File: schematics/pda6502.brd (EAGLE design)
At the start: 100 x 80 mm, 40 parts, among them IC1 74HC00D, IC2 74HC138D, IC3 DS1813-SMD, J1 CON_HEADER_2X07-PTH, U1 W65C02S, U2 W65C22S, U3 28C256, U4 UM61256AK-12

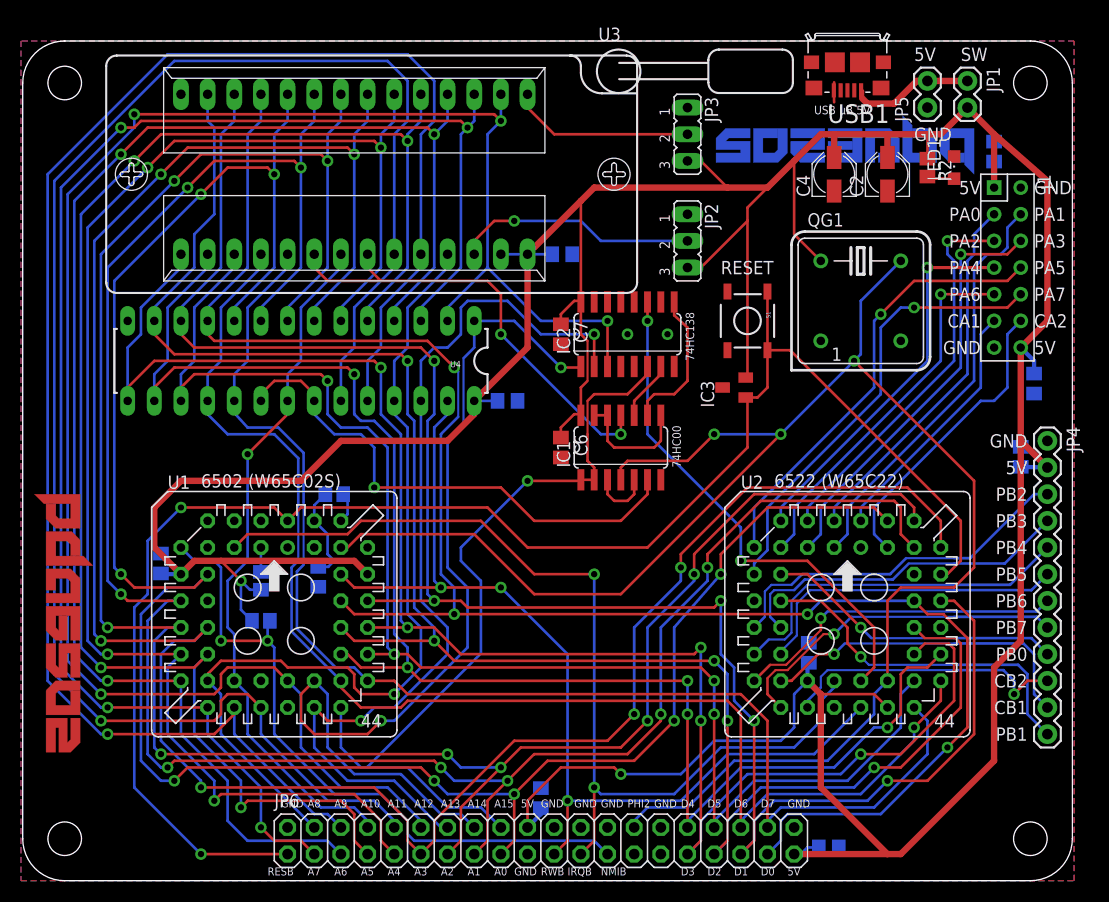
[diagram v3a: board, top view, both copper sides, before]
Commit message: board: silkscreen labelling; ~90% done.
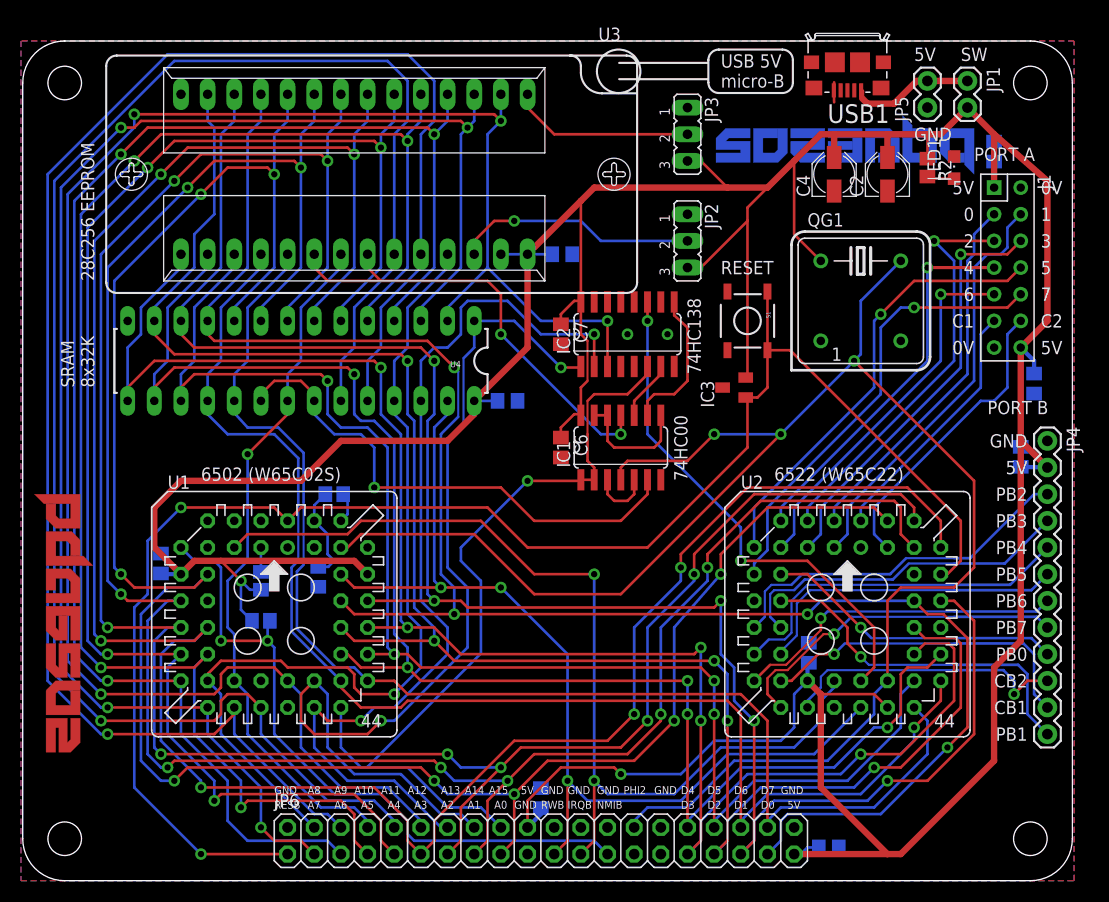
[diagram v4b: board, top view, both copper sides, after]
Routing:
- net PA2: track 37.2 -> 39.0 mm
- net RWB: track 94.5 -> 95.3 mm
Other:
- board text added: "0"
- board text added: "0V"
- board text added: "1"
- board text added: "2"
- board text added: "28C256 EEPROM"
- board text added: "3"
- board text added: "4"
- board text added: "5"
- board text added: "6"
- board text added: "7"
- board text added: "C1"
- board text added: "C2"
- board text added: "PORT A"
- board text added: "PORT B"
- board text added: "SRAM 8x32K"
- board text added: "USB 5V micro-B"
- board text removed: "CA1"
- board text removed: "CA2"
- board text removed: "PA0"
- board text removed: "PA1"
- board text removed: "PA2"
- board text removed: "PA3"
- board text removed: "PA4"
- board text removed: "PA5"
- board text removed: "PA6"
- board text removed: "PA7"
- board text removed: "USB µB 5V"

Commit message: schematics, board: labelling, tweaks, polish.
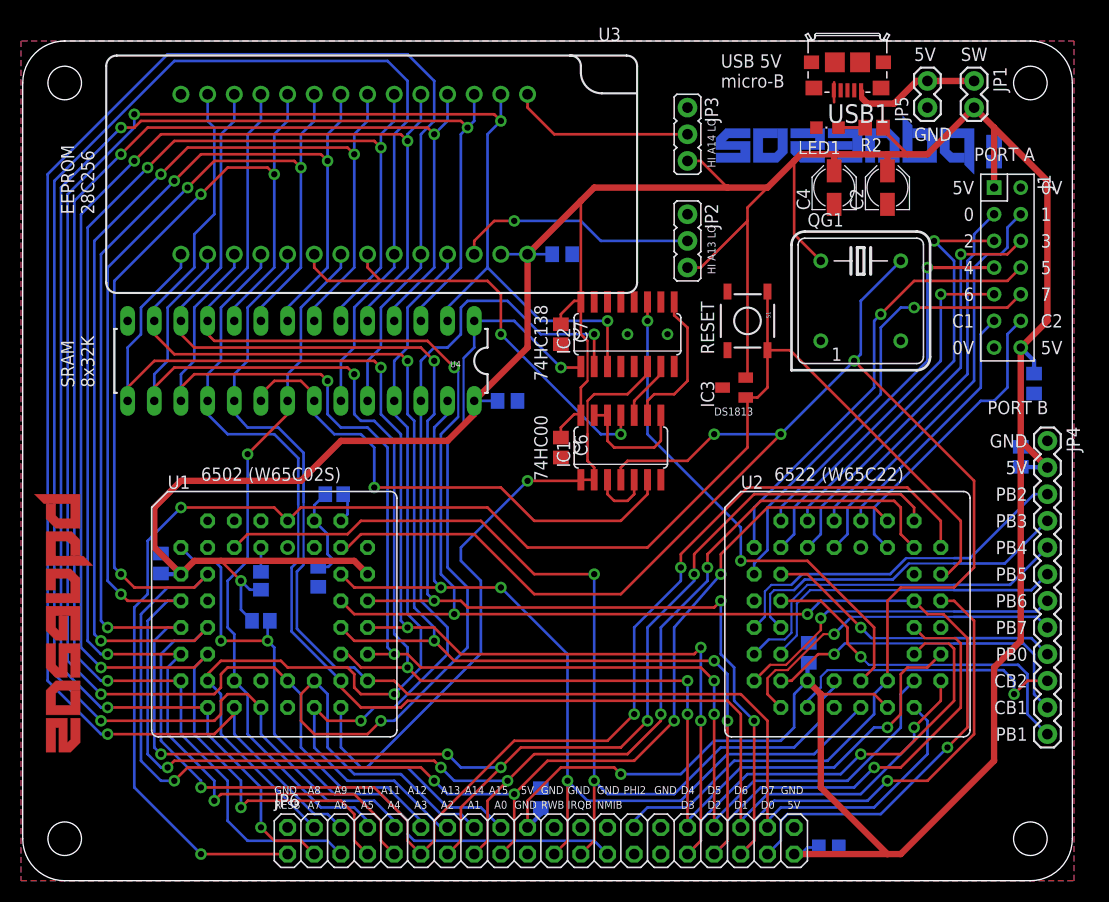
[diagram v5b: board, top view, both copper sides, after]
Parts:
- JP2, JP3: device jumper:JP2 -> pda:JP2
- moved LED1 12.7 mm to (76.8, 71.8), turned to 90 degrees
- moved R2 6.35 mm to (81.3, 71.8), turned to 180 degrees
- moved C2 1.27 mm to (82.5, 66.0)
- moved C4 1.27 mm to (77.5, 66.0)
- moved JP1 0.64 mm to (90.8, 76.2)
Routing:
- net 5V: track 409.9 -> 410.7 mm
- net N$4: track 11.9 -> 12.6 mm
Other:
- board text added: "DS1813"
- board text added: "EEPROM 28C256"
- board text added: "HI A13 LO"
- board text added: "HI A14 LO"
- board text removed: "28C256 EEPROM"

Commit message: board: round pads, not long; layout tweaks; polish.
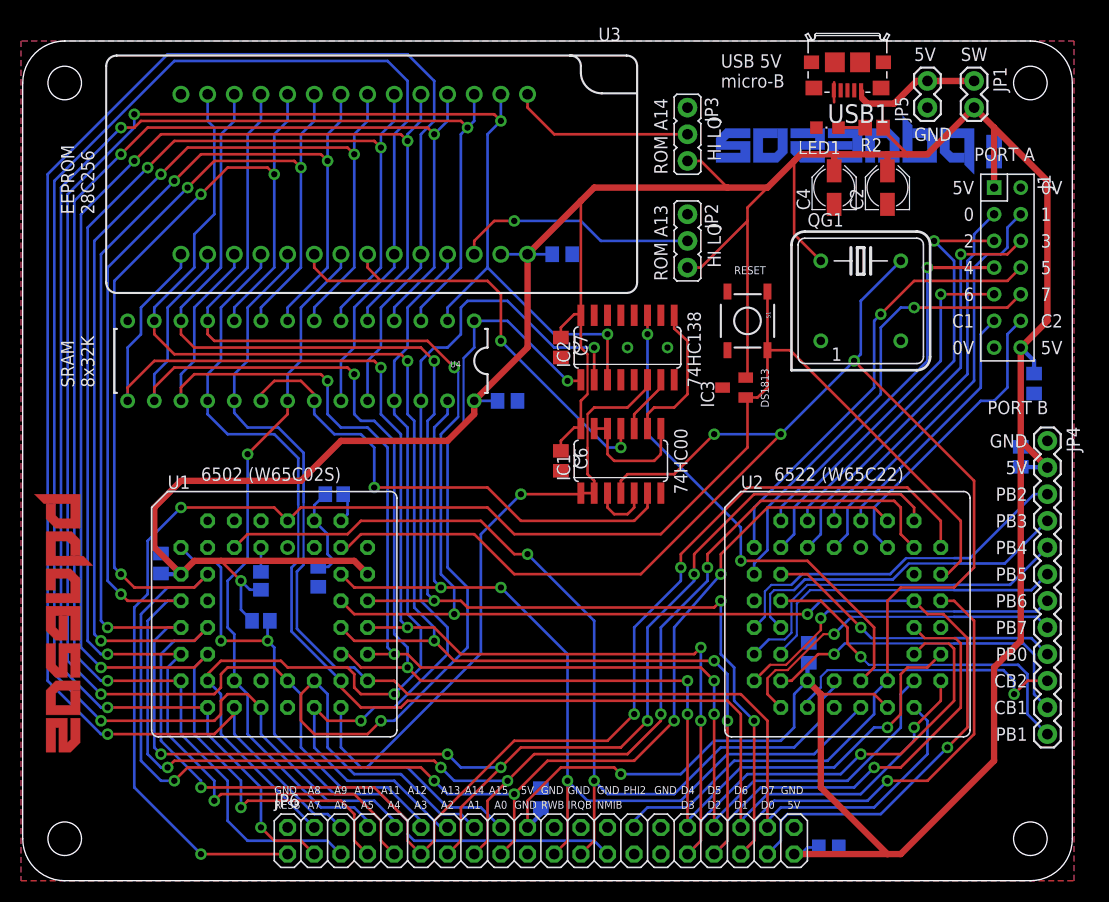
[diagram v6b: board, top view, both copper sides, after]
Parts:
- moved C7 1.27 mm to (51.4, 50.8)
- moved IC2 1.27 mm to (57.8, 50.8)
- moved C6 1.27 mm to (51.4, 40.0)
- moved IC1 1.27 mm to (57.1, 40.0)
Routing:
- net IRQB: track 94.0 -> 91.4 mm
- net ADDR15: track 79.1 -> 76.6 mm
- net 5V: track 410.7 -> 411.9 mm
- net VIA_CE: track 49.3 -> 48.0 mm
- net PHI2: track 163.1 -> 162.0 mm
- net RESB: track 154.1 -> 153.1 mm
- net ROM_CE: track 44.2 -> 45.1 mm
- net ADDR14: track 93.2 -> 93.7 mm
- net ADDR13: track 89.3 -> 89.8 mm
- net ADDR12: track 177.9 -> 178.4 mm
- net RAM_CE: track 49.3 -> 48.8 mm
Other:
- board text added: "HI LO"
- board text added: "ROM A13"
- board text added: "ROM A14"
- board text removed: "HI A13 LO"
- board text removed: "HI A14 LO"

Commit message: board: labelling, layout tweaks, polish.
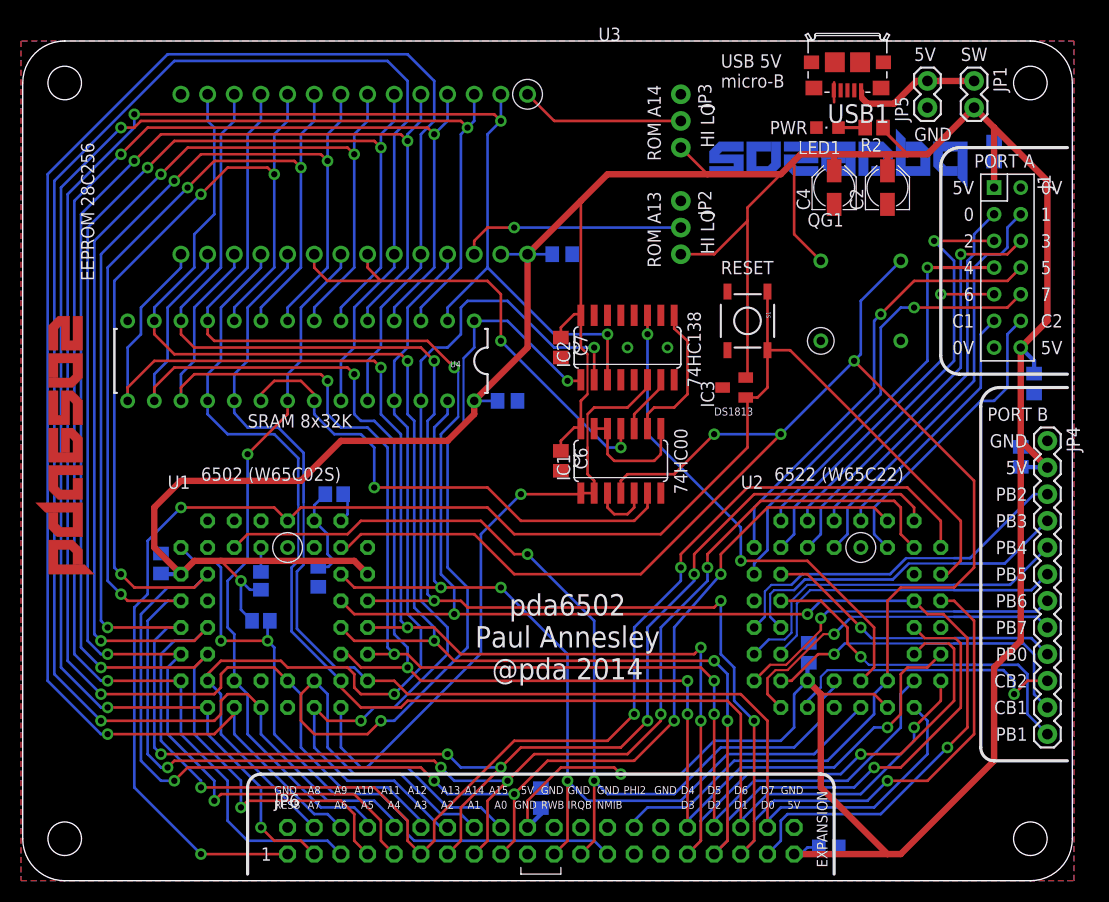
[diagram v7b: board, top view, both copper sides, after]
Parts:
- JP6: device adafruit:2X20 -> pda:2X20
- QG1: device crystal:DIL08S -> pda:DIL08S
- moved U$3 9.52 mm to (6.99, 29.2), turned to 90 degrees
- moved U$4 1.42 mm to (90.2, 66.0)
- moved JP2 1.42 mm to (62.9, 62.2)
- moved JP3 1.42 mm to (62.9, 72.4)
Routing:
- net N$6: track 17.6 -> 15.7 mm
- net N$10: track 23.2 -> 21.5 mm
- net 5V: track 411.9 -> 412.6 mm
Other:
- board text added: "EXPANSION"
- board text added: "PWR"
- board text added: "pda6502 Paul Annesley @pda 2014"

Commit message: board: spaced routing between PLCCs; more ground pour.
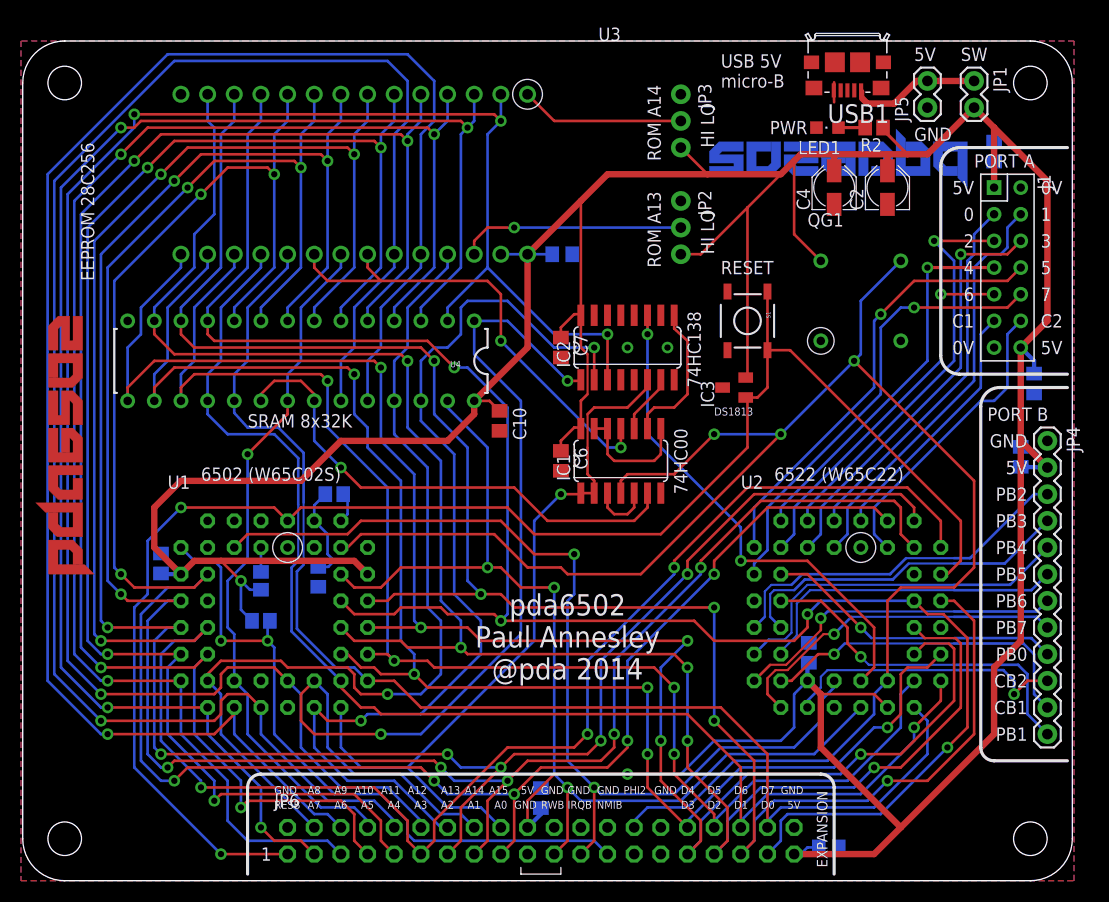
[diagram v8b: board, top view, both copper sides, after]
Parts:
- moved C10 2.05 mm to (45.6, 43.8), flipped to the top, turned to 270 degrees
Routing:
- net DATA0: track 170.5 -> 176.3 mm
- net ADDR13: track 89.8 -> 94.3 mm
- net ADDR14: track 93.7 -> 98.0 mm
- net ADDR15: track 76.6 -> 72.8 mm
- net DATA6: track 129.3 -> 125.8 mm
- net DATA5: track 137.4 -> 133.9 mm
- net RWB: track 95.3 -> 98.5 mm
- net ADDR8: track 85.3 -> 88.4 mm
- net 5V: track 412.6 -> 409.6 mm
- net IRQB: track 91.4 -> 94.3 mm
- net DATA4: track 149.8 -> 147.4 mm
- net DATA7: track 124.6 -> 122.7 mm
- net DATA3: track 163.8 -> 165.6 mm
- net ADDR3: track 221.2 -> 219.7 mm
- net ADDR2: track 208.3 -> 206.9 mm
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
